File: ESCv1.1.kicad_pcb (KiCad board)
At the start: 2 copper layers, 27.3 x 63.8 mm, 65 parts, among them J1 ST_SH_SM06B-SRSS-TB_1x06-1MP, J3_1 PWR_Pads, J3_2 PWR_IN, J4_1 Phase_Pads, J4_2 1x3 Header, Q1 BC847BTT1G, U1 DRV8316, U2 ArdunioMKR_Shield

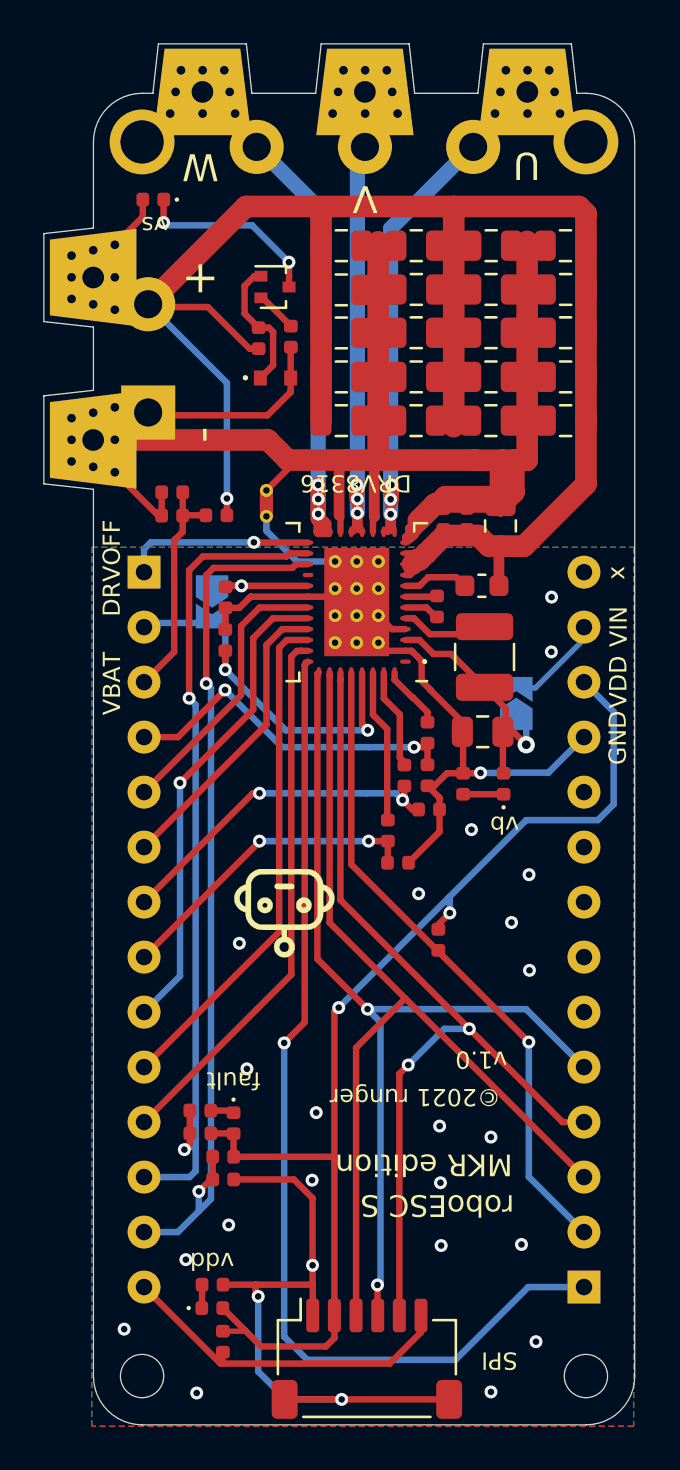
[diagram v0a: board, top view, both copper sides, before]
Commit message: v1.1 update, fixed pin assignment for nFAULT
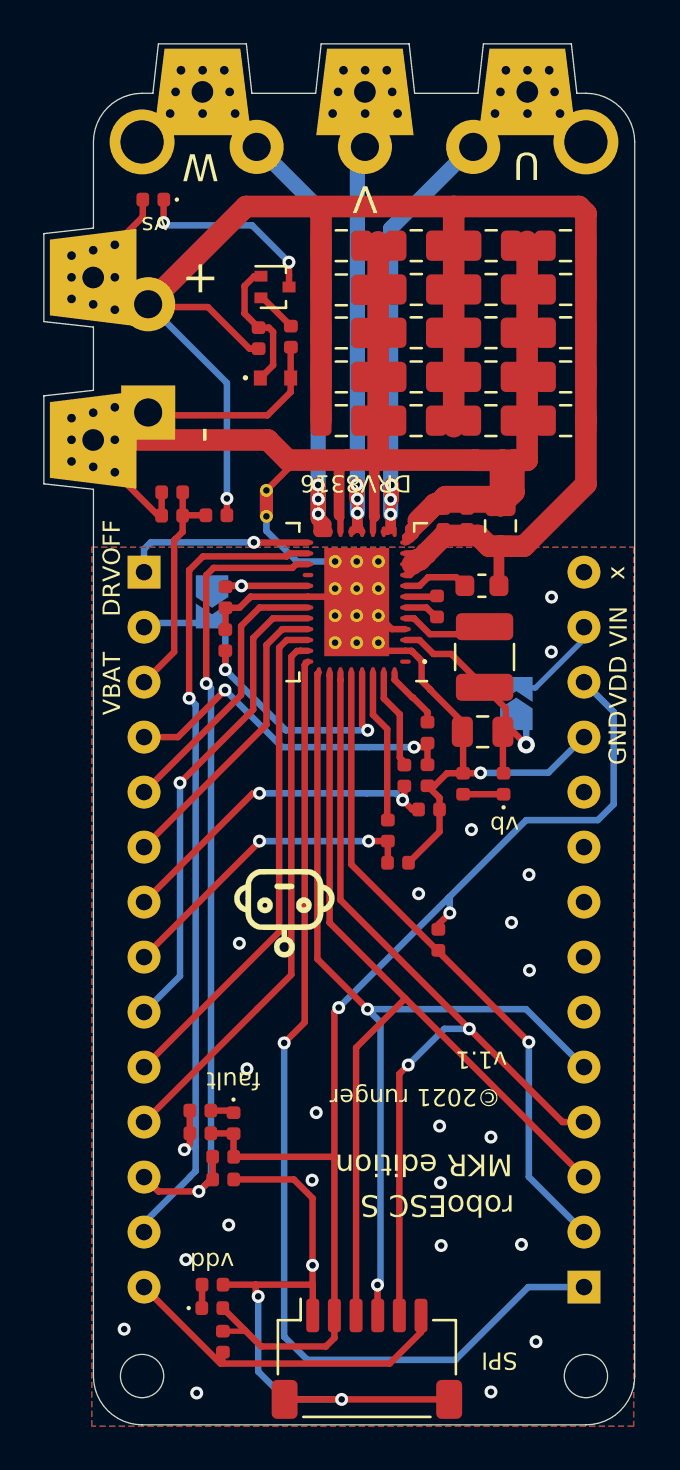
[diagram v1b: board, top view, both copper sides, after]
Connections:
- U2 pad 12: nFAULT -> nSLEEP
- U2 pad 13: nSLEEP -> nFAULT
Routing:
- net nSLEEP: track 40.3 -> 38.4 mm
- net nFAULT: track 38.7 -> 40.0 mm
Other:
- board text added: "v1.1"
- board text removed: "v1.0"
